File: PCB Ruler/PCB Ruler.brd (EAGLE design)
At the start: 76.2 x 12.7 mm, 1 part

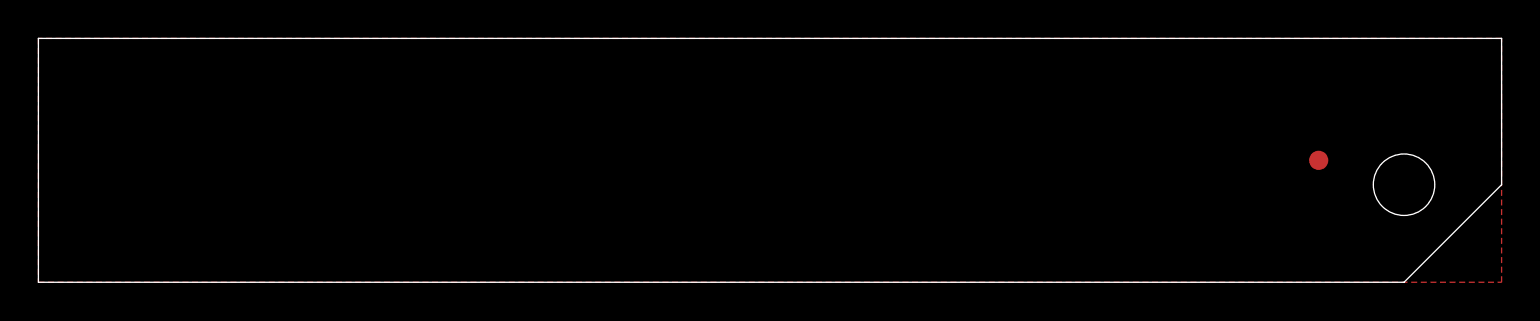
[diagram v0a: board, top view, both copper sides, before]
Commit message: Updated website on silkscreen
Signed-off-by: Cruz Monrreal II <Cruz.Monrreal@gmail.com>
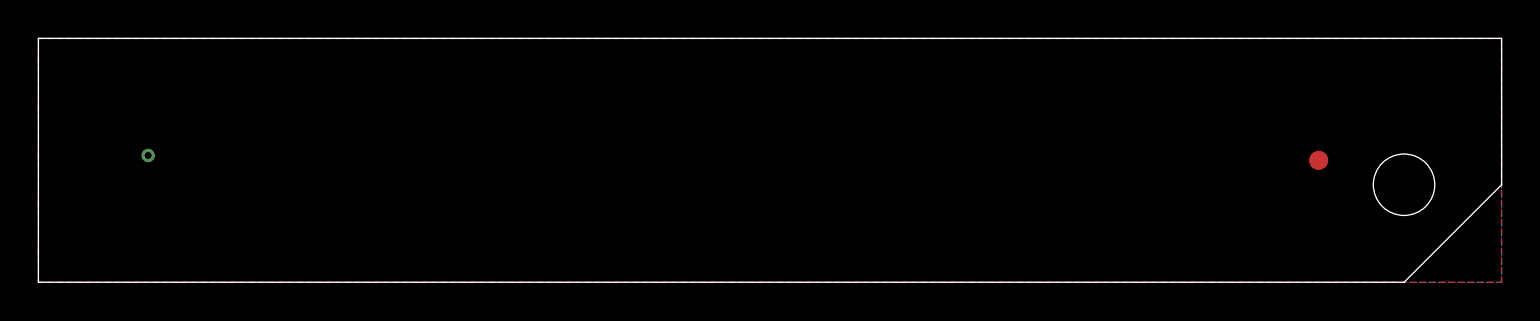
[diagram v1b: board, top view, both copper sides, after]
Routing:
- added copper zone on layer 1, net GND
- added copper zone on layer 16, net GND
- removed copper zone on layer 1, net N$1
